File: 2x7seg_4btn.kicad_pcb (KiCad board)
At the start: 2 copper layers, 64 x 26.3 mm, 61 parts, among them CON1 AVR-ISP, IC1 ATTINY88-A, Q1 2N7002, Q2 2N7002, Q3 2N7002, Q4 2N7002, U1 74HC14D_653, U10 MC14543B, U11 MC14543B, U2 SW_SPST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

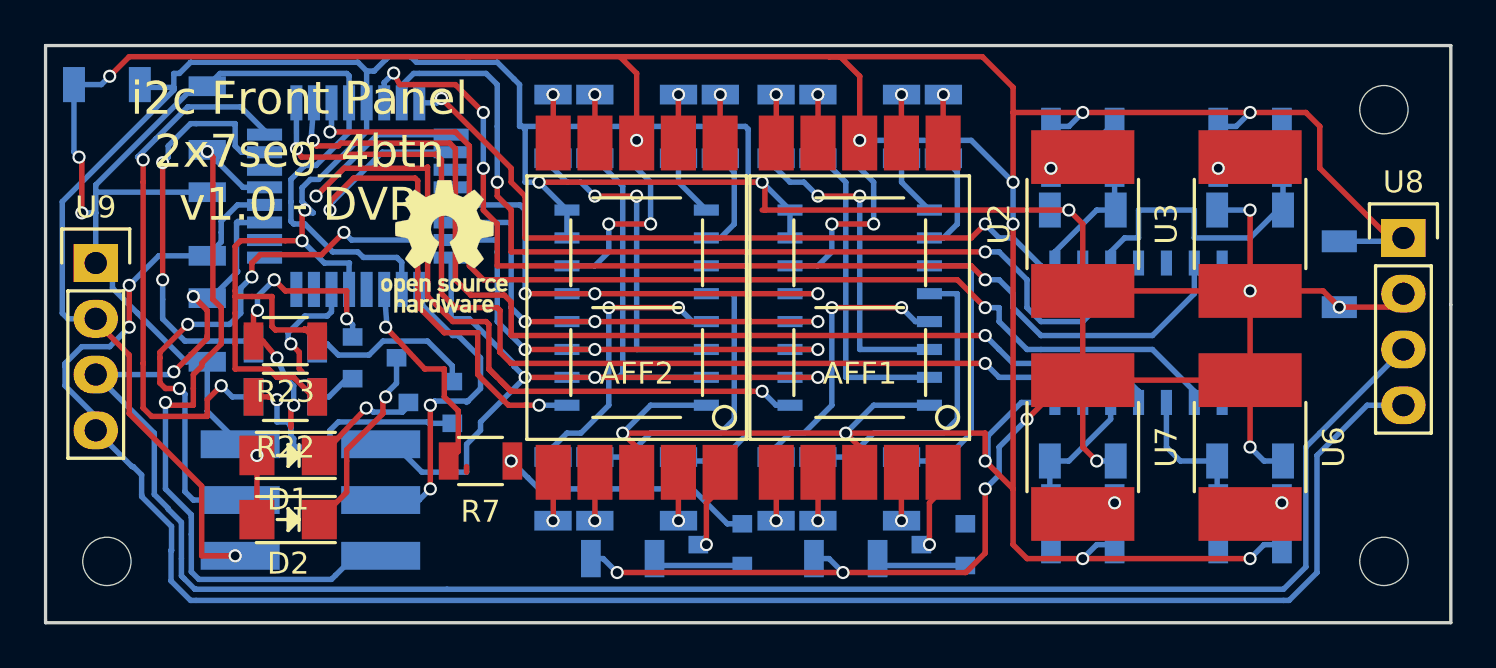
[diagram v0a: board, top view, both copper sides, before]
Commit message: Headers aligned better
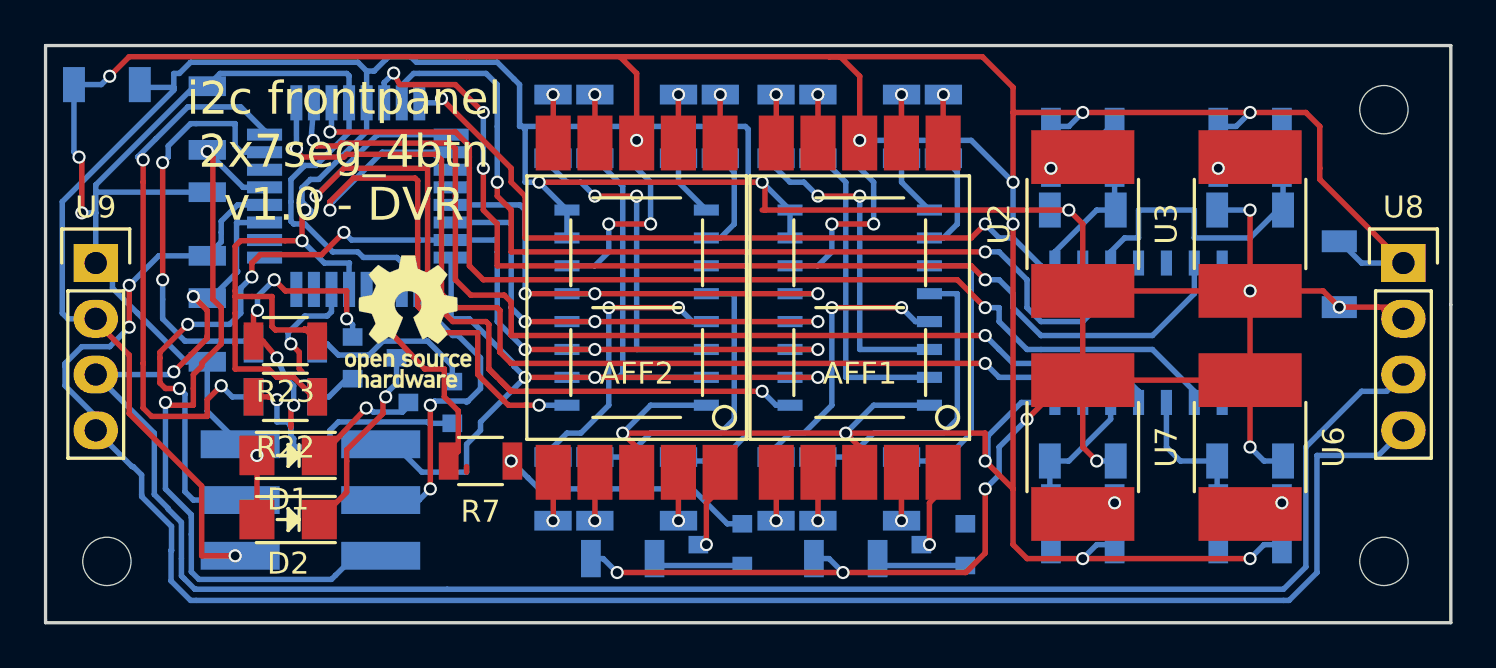
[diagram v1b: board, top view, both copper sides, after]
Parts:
- moved REF*** 3.81 mm to (49.3, 33.7)
- moved U8 1.14 mm to (94.6, 31.0)
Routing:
- net VCC: track 240.4 -> 241.5 mm
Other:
- board text added: "i2c frontpanel 2x7seg_4btn v1.0 - DVR"
- board text removed: "i2c Front Panel 2x7seg_4btn v1.0 - DVR"
